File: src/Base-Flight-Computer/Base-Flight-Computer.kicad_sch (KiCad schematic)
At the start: 51 parts, among them J1 Jumper_NO, P1 1984659, P2 USB, P3 0530470610, P4 1546551-2, Q1 QS5U17TR, Q2 2N7002W-7-F, Q3 2N7002W-7-F, Q4 QS5U17TR, U1 STM32G4A1KEU6, U2 BMP390, U3 LMS8117AMP-3.3_NOPB, Y1 ECS-240-18-33-JGN-TR

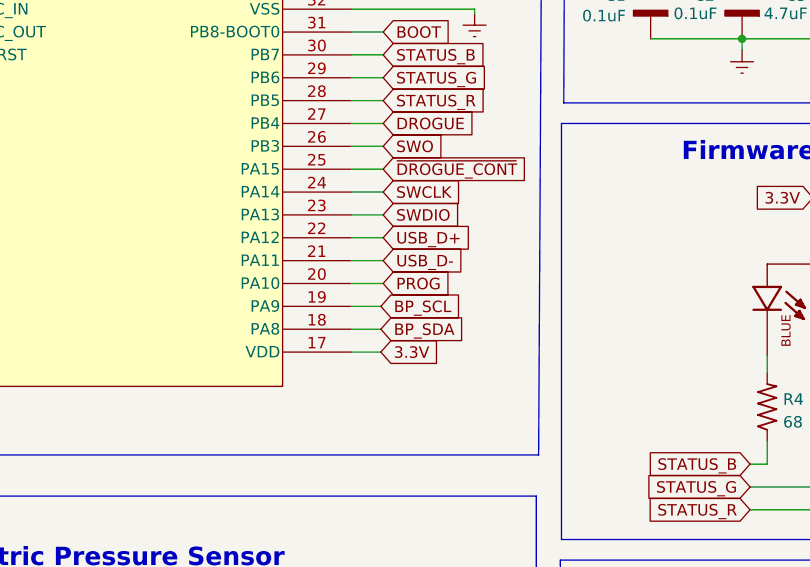
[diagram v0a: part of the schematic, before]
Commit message: removed programming button
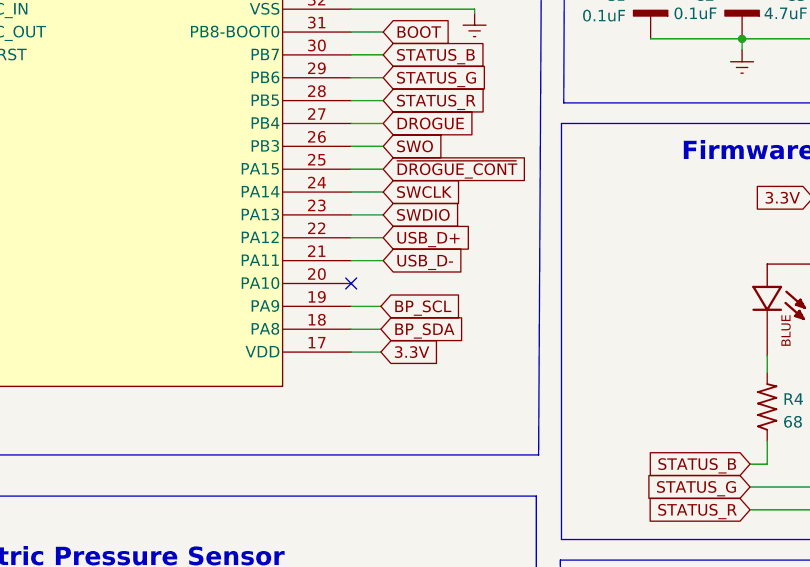
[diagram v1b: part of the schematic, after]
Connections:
- net PROG: no longer names the net of U1.20 (PA10)
- no-connect marks 3 -> 4

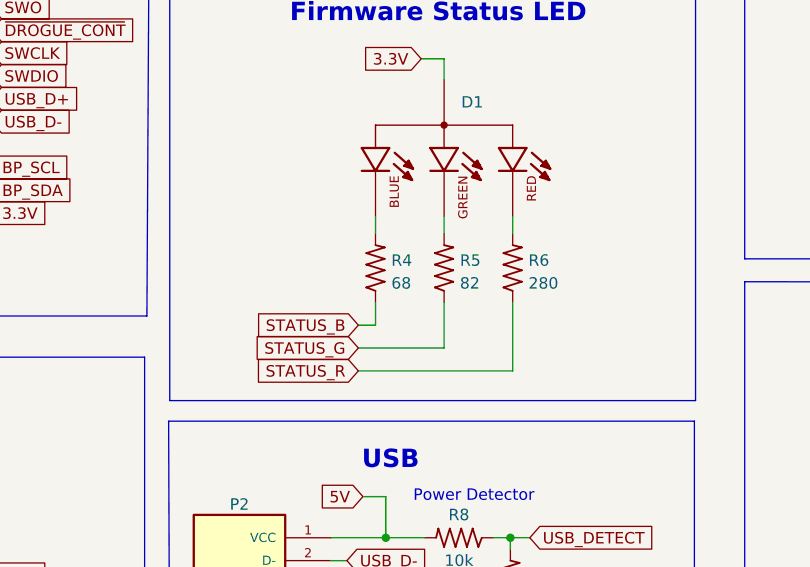
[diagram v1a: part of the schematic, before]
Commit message: increased blue LED resistance
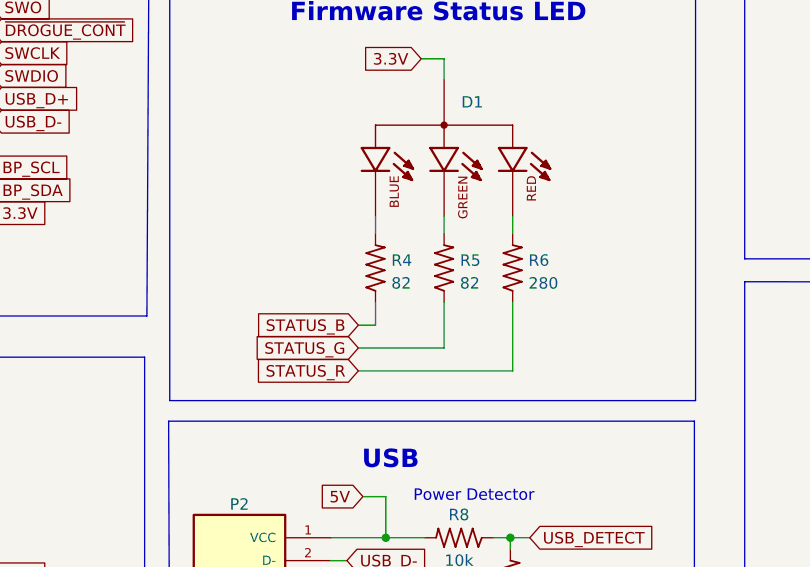
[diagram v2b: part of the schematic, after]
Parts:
- R4: value 68 -> 82
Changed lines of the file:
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@@
       (effects (font (size 1.27 1.27)) (justify right))
     )
-    (property "Value" "68" (at 138.9126 80.9502 90)
+    (property "Value" "82" (at 138.9126 80.9502 90)
       (effects (font (size 1.27 1.27)) (justify right))
     )

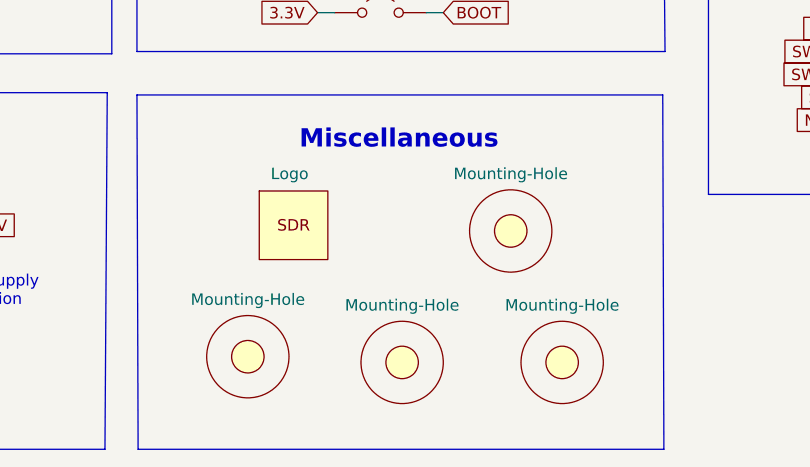
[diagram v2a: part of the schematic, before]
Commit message: updated schematic links to new library files
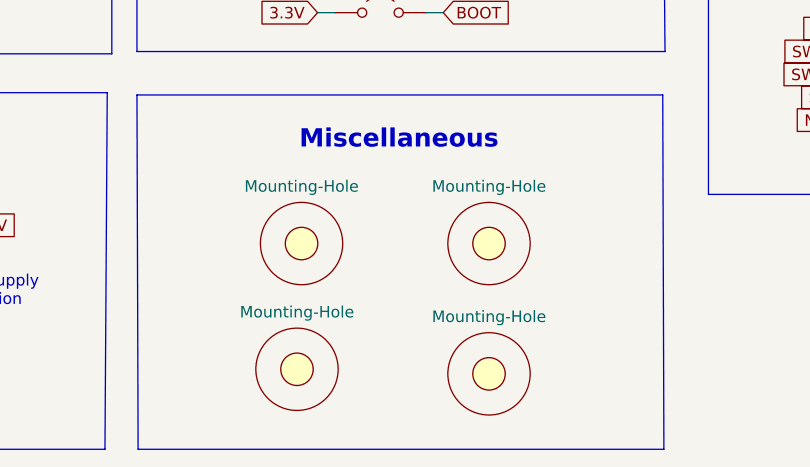
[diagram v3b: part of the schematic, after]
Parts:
- removed LOGO1: Logo, Flight-Computer-Lite:logo_small, symbol Flight-Computer:Logo
- D1: footprint Flight-Computer-Lite:CLMVC-FKA-CL1D1L71BB7C3C3 -> LED_CLMVC-FKA-CL1D1L71BB7C3C3
- D2, D4: footprint Flight-Computer-Lite:SM5819PL-TP -> SOD-123FL_MCC
- J1: footprint Flight-Computer-Lite:Jumper-NO -> Engine-Controller:Jumper-NO
- P1: footprint Flight-Computer-Lite:1984659 -> Flight-Computer:1984659
- P3: footprint Flight-Computer-Lite:53047-0610 -> Flight-Computer-Lite:3220-20-0200-00
- P4: footprint Flight-Computer-Lite:1546551-2 -> Flight-Computer:1546551-2
- Q1, Q4: footprint Flight-Computer-Lite:QS5U17TR -> Flight-Computer:QS5U17TR
- Q2, Q3: footprint Flight-Computer-Lite:2N7002W-7-F -> Flight-Computer-Lite:QS5U17TR
- U1: footprint Flight-Computer-Lite:STM32G4A1KEU6 -> QFPN_4A1KEU6_STM
- U2: footprint Flight-Computer-Lite:BMP390 -> XDCR_BMP390L

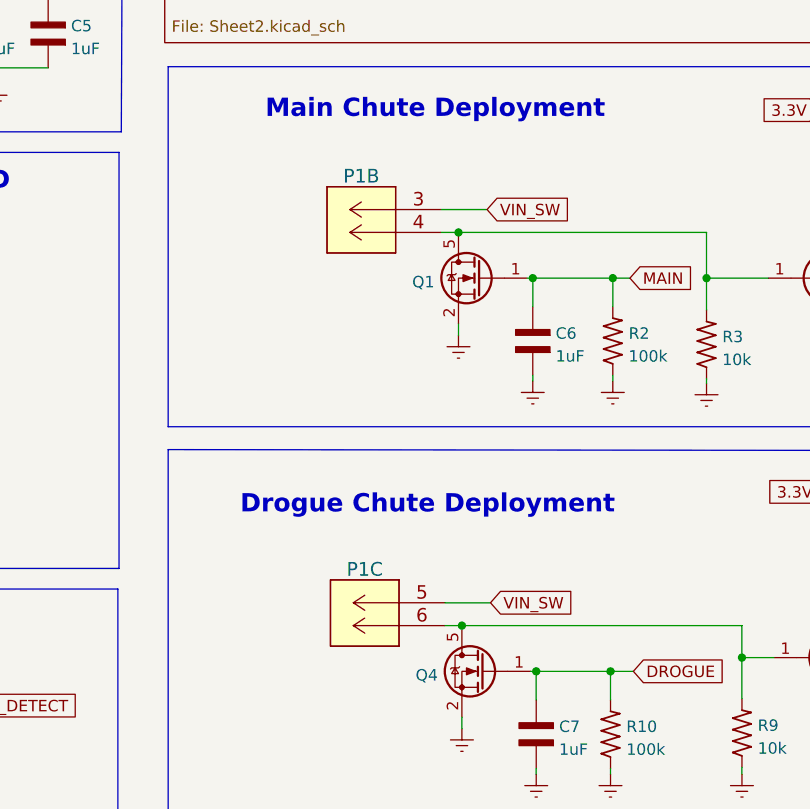
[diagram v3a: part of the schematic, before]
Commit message: added new screw terminals to schematic
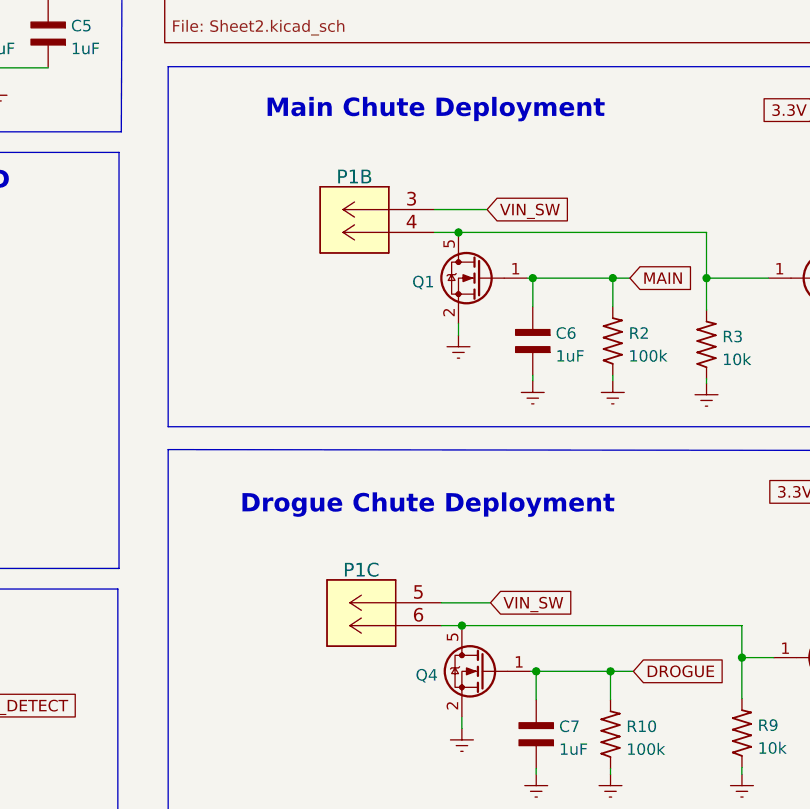
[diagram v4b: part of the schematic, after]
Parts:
- removed P1: 1984659, Flight-Computer:1984659, symbol Flight-Computer:1984659
- added P1: 1984659, Base-Flight-Computer:1984659, symbol Base-Flight-Computer:284391-6
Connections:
- net VIN_SW: now also P1.3 (5), P1.5
- net at Q1.5 (D), Q2.1 (G), R3.2: now also P1.4 (6)
- net at Q3.1 (G), Q4.5 (D), R9.2: now also P1.6

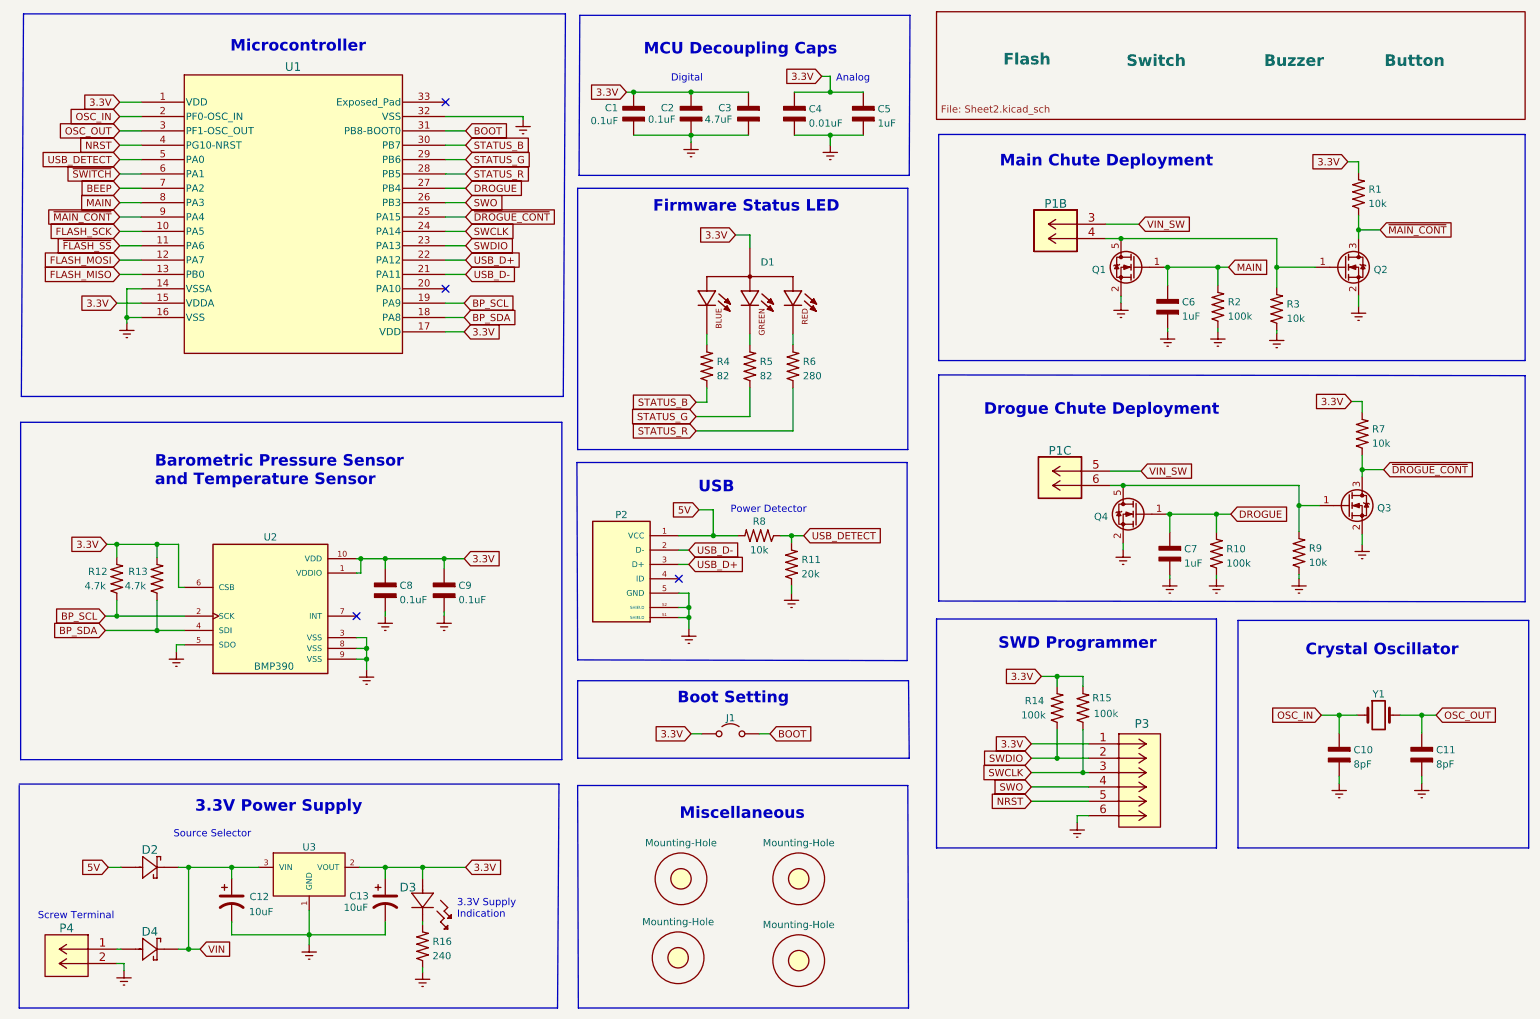
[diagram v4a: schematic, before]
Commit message: updated schematic with 0402 resistors and capacitors
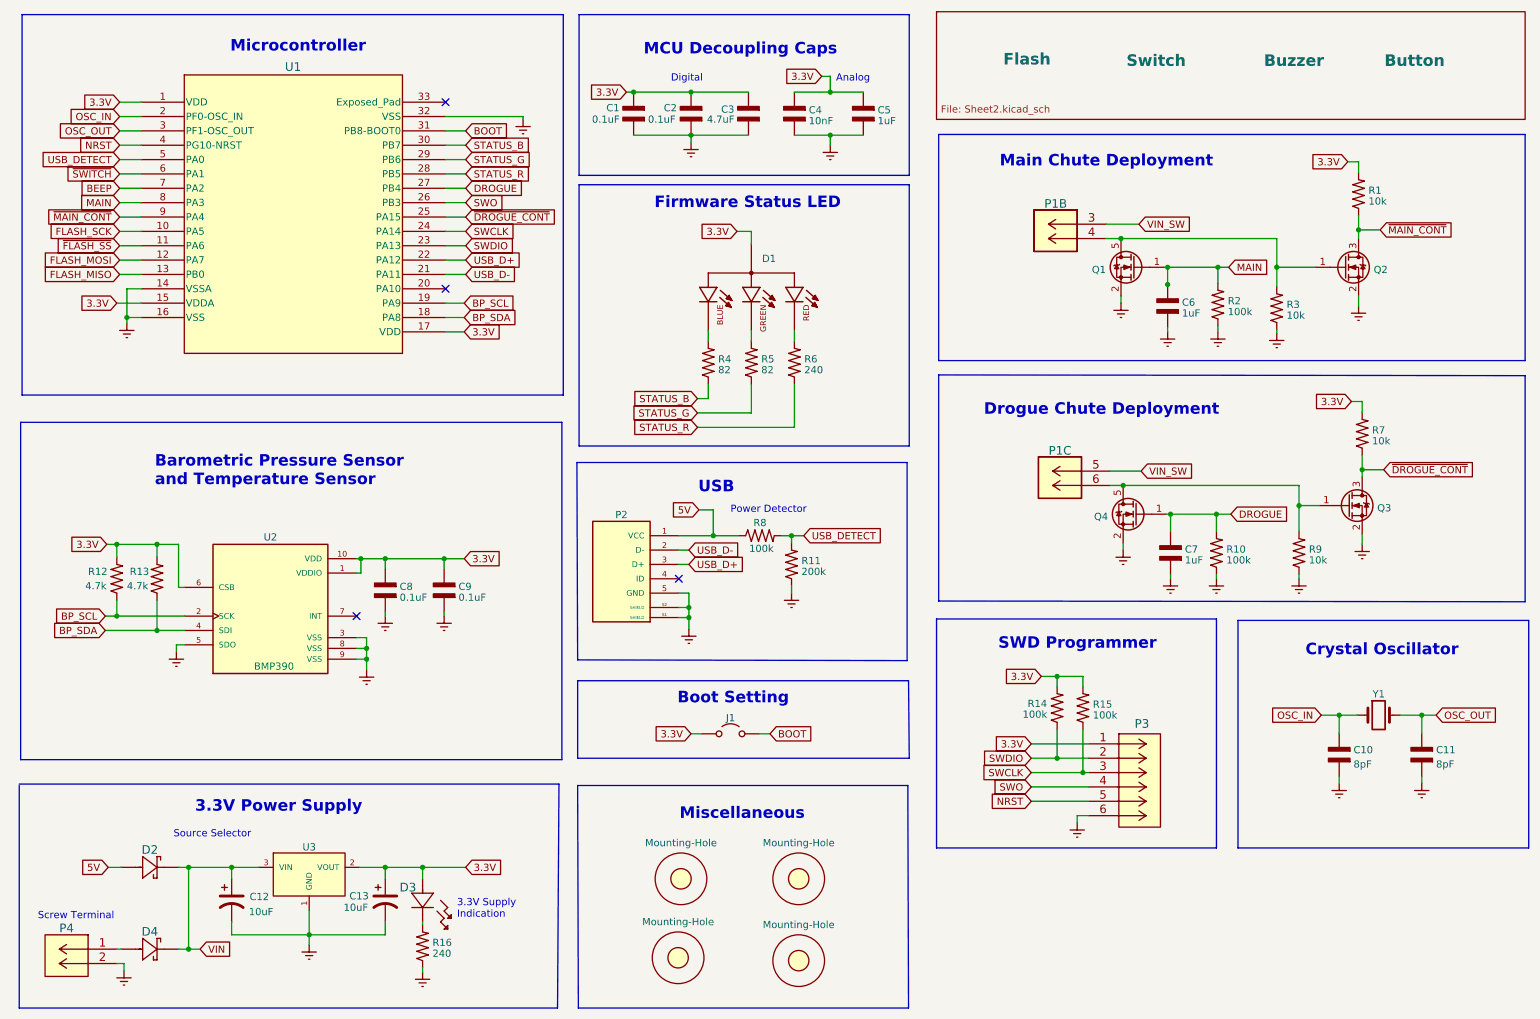
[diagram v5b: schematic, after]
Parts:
- removed C1, C2, C8, C9: 0.1uF, Flight-Computer-Lite:CAP_0603, symbol Flight-Computer:CAP_0603
- removed C3: 4.7uF, Flight-Computer-Lite:CAP_0603, symbol Flight-Computer:CAP_0603
- removed C4: 0.01uF, Flight-Computer-Lite:CAP_0603, symbol Flight-Computer:CAP_0603
- removed C5, C6, C7: 1uF, Flight-Computer-Lite:CAP_0603, symbol Flight-Computer:CAP_0603
- removed R1, R3, R7, R8, R9: 10k, Flight-Computer-Lite:RES_0603, symbol Flight-Computer:RES_0603
- removed R10, R14, R15, R2: 100k, Flight-Computer-Lite:RES_0603, symbol Flight-Computer:RES_0603
- removed R11: 20k, Flight-Computer-Lite:RES_0603, symbol Flight-Computer:RES_0603
- removed R12, R13: 4.7k, Flight-Computer-Lite:RES_0603, symbol Flight-Computer:RES_0603
- removed R16: 240, Flight-Computer-Lite:RES_0603, symbol Flight-Computer:RES_0603
- removed R4, R5: 82, Flight-Computer-Lite:RES_0603, symbol Flight-Computer:RES_0603
- removed R6: 280, Flight-Computer-Lite:RES_0603, symbol Flight-Computer:RES_0603
- added C1, C2, C8, C9: 0.1uF, Base-Flight-Computer:CAP_0402, symbol Base-Flight-Computer:CAP_0402
- added C3: 4.7uF, Base-Flight-Computer:CAP_0402, symbol Base-Flight-Computer:CAP_0402
- added C4: 10nF, Base-Flight-Computer:CAP_0402, symbol Base-Flight-Computer:CAP_0402
- added C5, C6, C7: 1uF, Base-Flight-Computer:CAP_0402, symbol Base-Flight-Computer:CAP_0402
- added R1, R3, R7, R9: 10k, Base-Flight-Computer:RES_0402, symbol Base-Flight-Computer:RES_0402
- added R10, R14, R15, R2, R8: 100k, Base-Flight-Computer:RES_0402, symbol Base-Flight-Computer:RES_0402
- added R11: 200k, Base-Flight-Computer:RES_0402, symbol Base-Flight-Computer:RES_0402
- added R12, R13: 4.7k, Base-Flight-Computer:RES_0402, symbol Base-Flight-Computer:RES_0402
- added R16, R6: 240, Base-Flight-Computer:RES_0402, symbol Base-Flight-Computer:RES_0402
- added R4, R5: 82, Base-Flight-Computer:RES_0402, symbol Base-Flight-Computer:RES_0402
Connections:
- net 3.3V: now also C1.1, C2.1, C3.1, C4.1, C5.1, C8.1, C9.1, R1.2, R12.2, R13.2, R14.2, R15.2, R7.2
- net 5V: now also R8.1
- net BP_SCL: now also R12.1
- net BP_SDA: now also R13.1
- net DROGUE: now also C7.1, R10.2
- net Earth: now also C1.2, C2.2, C3.2, C4.2, C5.2, C6.2, C7.2, C8.2, C9.2, R10.1, R11.1, R16.1, R2.1, R3.1, R9.1
- net MAIN: now also C6.1, R2.2
- net STATUS_B: now also R4.1
- net STATUS_G: now also R5.1
- net STATUS_R: now also R6.1
- net SWCLK: now also R15.1
- net SWDIO: now also R14.1
- net USB_DETECT: now also R11.2, R8.2
- net ~{DROGUE_CONT}: now also R7.1
- net ~{MAIN_CONT}: now also R1.1
- net at P1.4 (6), Q1.5 (D), Q2.1 (G): now also R3.2
- net at D3.1: now also R16.2
- net at P1.6, Q3.1 (G), Q4.5 (D): now also R9.2
- net at D1.4: now also R6.2
- net at D1.3: now also R5.2
- net at D1.2: now also R4.2
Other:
- moved on the sheet: D1
